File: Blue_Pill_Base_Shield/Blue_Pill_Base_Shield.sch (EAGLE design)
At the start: 10 parts, among them J1 4P-2.0, J2 4P-2.0, J3 4P-2.0, J4 4P-2.0, J5 4P-2.0, J6 4P-2.0, J7 4P-2.0, J8 4P-2.0

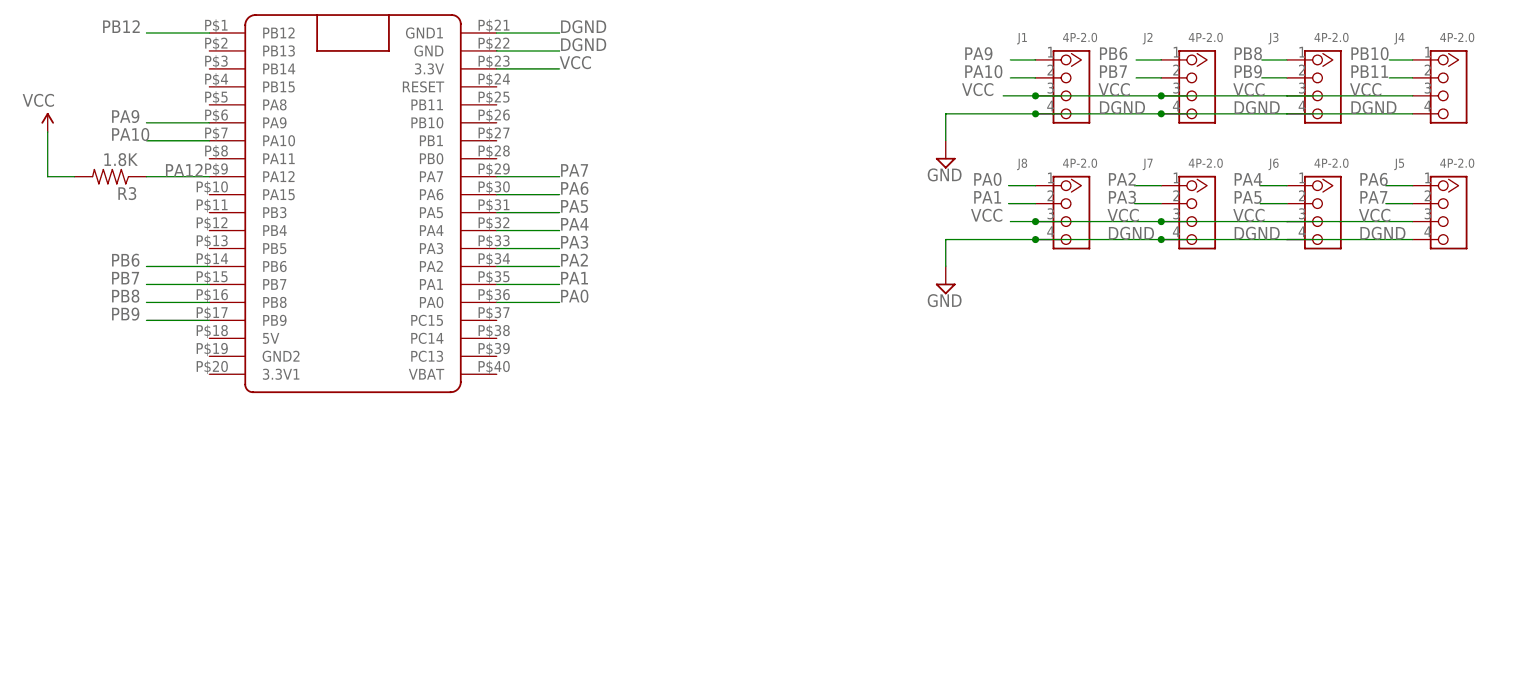
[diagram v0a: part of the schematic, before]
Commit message: Update Blue Pill Shield to add UART header
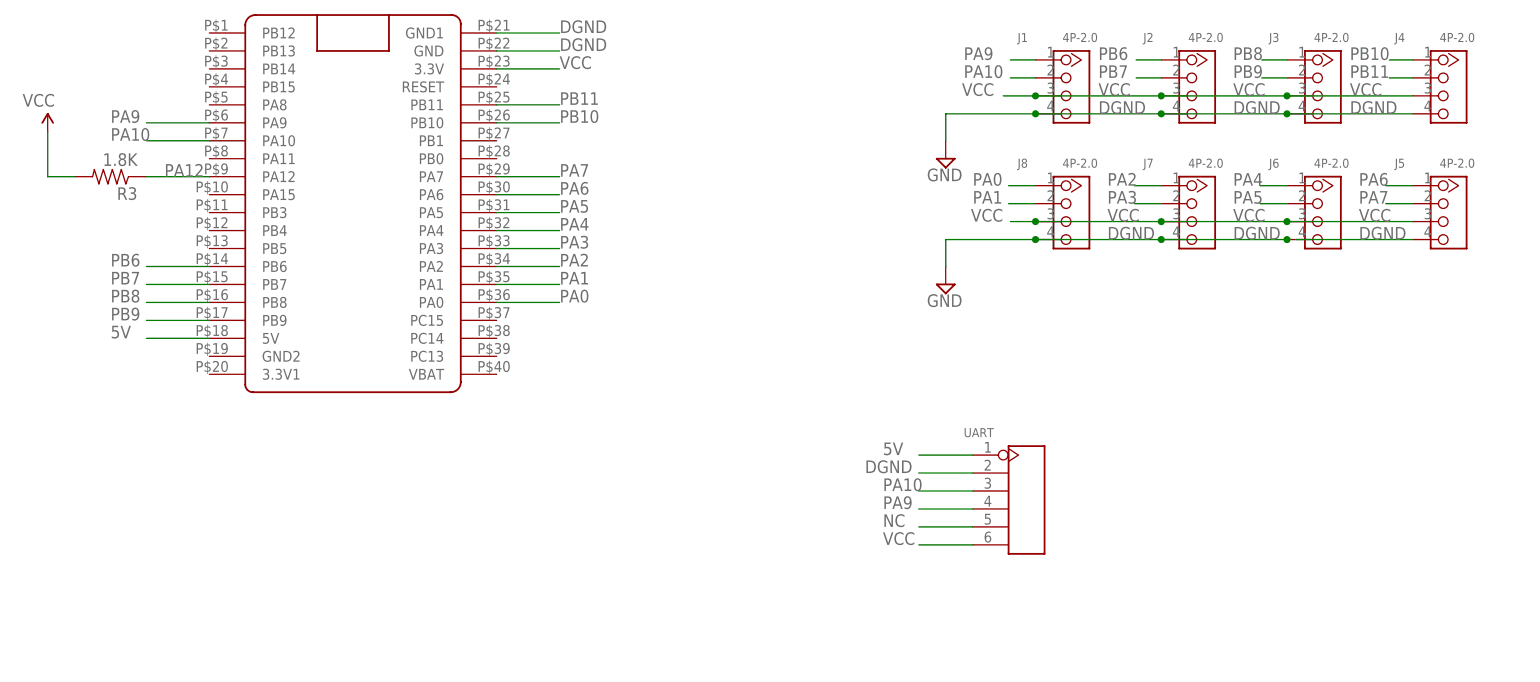
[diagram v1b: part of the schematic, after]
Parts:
- added UART: YELLOW-6P-2.54, Seeed-Connector:DIP-YELLOW-FEMALE-HEADER-VERT(6P-2.54)
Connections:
- removed net PB12: U$5.PB12
- new net 5V: U$5.5V, UART.1
- new net NC: UART.5
- net DGND: now also UART.2
- net PA10: now also UART.3
- net PA9: now also UART.4
- net PB10: now also U$5.PB10
- net PB11: now also U$5.PB11
- net VCC: now also UART.6
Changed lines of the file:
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@@
 <part name="J4" library="Seeed-Connector" library_urn="urn:adsk.eagle:library:478" deviceset="GROVE-CONNECTOR-DIP(4P-2.0)" device="" package3d_urn="urn:adsk.eagle:package:33111/1" value="4P-2.0"/>
 <part name="J5" library="Seeed-Connector" library_urn="urn:adsk.eagle:library:478" deviceset="GROVE-CONNECTOR-DIP(4P-2.0)" device="" package3d_urn="urn:adsk.eagle:package:33111/1" value="4P-2.0"/>
+<part name="UART" library="Seeed-Connector" deviceset="DIP-YELLOW-FEMALE-HEADER-VERT(6P-2.54)" device="" value="YELLOW-6P-2.54"/>
 </parts>
 <sheets>
@@
 <instance part="J4" gate="G$1" x="300.99" y="231.14"/>
 <instance part="J5" gate="G$1" x="300.99" y="213.36"/>
+<instance part="UART" gate="G$1" x="242.57" y="172.72" smashed="yes">
+<attribute name="NAME" x="233.68" y="181.61" size="1.27" layer="95" ratio="10"/>
+</instance>
 </instances>
 <busses>
@@
 <label x="271.78" y="212.09" size="1.778" layer="95"/>
 <label x="254" y="212.09" size="1.778" layer="95"/>
+<wire x1="297.18" y1="212.09" x2="279.4" y2="212.09" width="0.1524" layer="91"/>
+<pinref part="J5" gate="G$1" pin="3"/>
+<label x="289.56" y="212.09" size="1.778" layer="95"/>
+<junction x="279.4" y="212.09"/>
 </segment>
 <segment>
@@
 <label x="252.73" y="229.87" size="1.778" layer="95"/>
 <label x="271.78" y="229.87" size="1.778" layer="95"/>
+<wire x1="297.18" y1="229.87" x2="279.4" y2="229.87" width="0.1524" layer="91"/>
+<pinref part="J4" gate="G$1" pin="3"/>
+<label x="288.29" y="229.87" size="1.778" layer="95"/>
+<junction x="279.4" y="229.87"/>
 </segment>
 <segment>
@@
 </segment>
 <segment>
-<wire x1="297.18" y1="212.09" x2="279.4" y2="212.09" width="0.1524" layer="91"/>
-<pinref part="J5" gate="G$1" pin="3"/>
-<label x="289.56" y="212.09" size="1.778" layer="95"/>
-</segment>
-<segment>
-<wire x1="297.18" y1="229.87" x2="279.4" y2="229.87" width="0.1524" layer="91"/>
-<pinref part="J4" gate="G$1" pin="3"/>
-<label x="288.29" y="229.87" size="1.778" layer="95"/>
+<pinref part="UART" gate="G$1" pin="6"/>
+<wire x1="234.95" y1="166.37" x2="227.33" y2="166.37" width="0.1524" layer="91"/>
+<label x="222.25" y="166.37" size="1.778" layer="95"/>
 </segment>
 </net>
@@
 <label x="271.78" y="209.55" size="1.778" layer="95"/>
 <label x="254" y="209.55" size="1.778" layer="95"/>
+<junction x="279.4" y="209.55"/>
 </segment>
 <segment>
@@
 <label x="252.73" y="227.33" size="1.778" layer="95"/>
 <label x="271.78" y="227.33" size="1.778" layer="95"/>
+<wire x1="297.18" y1="227.33" x2="279.4" y2="227.33" width="0.1524" layer="91"/>
+<pinref part="J4" gate="G$1" pin="4"/>
+<label x="288.29" y="227.33" size="1.778" layer="95"/>
+<junction x="279.4" y="227.33"/>
 </segment>
 <segment>
@@
 </segment>
 <segment>
-<wire x1="297.18" y1="227.33" x2="279.4" y2="227.33" width="0.1524" layer="91"/>
-<pinref part="J4" gate="G$1" pin="4"/>
-<label x="288.29" y="227.33" size="1.778" layer="95"/>
-</segment>
-<segment>
-<wire x1="297.18" y1="209.55" x2="279.4" y2="209.55" width="0.1524" layer="91"/>
+<wire x1="297.18" y1="209.55" x2="280.67" y2="209.55" width="0.1524" layer="91"/>
 <pinref part="J5" gate="G$1" pin="4"/>
 <label x="289.56" y="209.55" size="1.778" layer="95"/>
+</segment>
+<segment>
+<pinref part="UART" gate="G$1" pin="2"/>
+<wire x1="234.95" y1="176.53" x2="227.33" y2="176.53" width="0.1524" layer="91"/>
+<label x="219.71" y="176.53" size="1.778" layer="95"/>
 </segment>
 </net>
@@
 <label x="113.03" y="226.06" size="1.778" layer="95"/>
 </segment>
+<segment>
+<pinref part="UART" gate="G$1" pin="4"/>
+<wire x1="234.95" y1="171.45" x2="227.33" y2="171.45" width="0.1524" layer="91"/>
+<label x="222.25" y="171.45" size="1.778" layer="95"/>
+</segment>
 </net>
 <net name="PA10" class="0">
@@
 <label x="113.03" y="223.52" size="1.778" layer="95"/>
 </segment>
+<segment>
+<pinref part="UART" gate="G$1" pin="3"/>
+<wire x1="234.95" y1="173.99" x2="227.33" y2="173.99" width="0.1524" layer="91"/>
+<label x="222.25" y="173.99" size="1.778" layer="95"/>
+</segment>
 </net>
 <net name="PB6" class="0">
@@
 <label x="288.29" y="234.95" size="1.778" layer="95"/>
 </segment>
+<segment>
+<pinref part="U$5" gate="G$1" pin="PB10"/>
+<wire x1="167.64" y1="226.06" x2="176.53" y2="226.06" width="0.1524" layer="91"/>
+<label x="176.53" y="226.06" size="1.778" layer="95"/>
+</segment>
 </net>
 <net name="PB11" class="0">
@@
 <wire x1="297.18" y1="232.41" x2="293.878" y2="232.41" width="0.1524" layer="91"/>
 <label x="288.29" y="232.41" size="1.778" layer="95"/>
+</segment>
+<segment>
+<pinref part="U$5" gate="G$1" pin="PB11"/>
+<wire x1="167.64" y1="228.6" x2="176.53" y2="228.6" width="0.1524" layer="91"/>
+<label x="176.53" y="228.6" size="1.778" layer="95"/>
 </segment>
 </net>
@@
 </segment>
 </net>
-<net name="PB12" class="0">
-<segment>
-<wire x1="118.11" y1="238.76" x2="127" y2="238.76" width="0.1524" layer="91"/>
-<label x="111.76" y="238.76" size="1.778" layer="95"/>
-<pinref part="U$5" gate="G$1" pin="PB12"/>
+<net name="5V" class="0">
+<segment>
+<pinref part="UART" gate="G$1" pin="1"/>
+<wire x1="234.95" y1="179.07" x2="227.33" y2="179.07" width="0.1524" layer="91"/>
+<label x="222.25" y="179.07" size="1.778" layer="95"/>
+</segment>
+<segment>
+<pinref part="U$5" gate="G$1" pin="5V"/>
+<wire x1="127" y1="195.58" x2="118.11" y2="195.58" width="0.1524" layer="91"/>
+<label x="113.03" y="195.58" size="1.778" layer="95"/>
+</segment>
+</net>
+<net name="NC" class="0">
+<segment>
+<pinref part="UART" gate="G$1" pin="5"/>
+<wire x1="234.95" y1="168.91" x2="227.33" y2="168.91" width="0.1524" layer="91"/>
+<label x="222.25" y="168.91" size="1.778" layer="95"/>
 </segment>
 </net>
@@
 </sheet>
 </sheets>
+<errors>
+</errors>
 </schematic>
 </drawing>
